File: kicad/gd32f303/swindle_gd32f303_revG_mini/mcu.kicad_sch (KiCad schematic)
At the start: 23 parts, among them J40 J40, J7 Conn_01x05_Pin, Q1 DMG2302U, U1 GD32F303, Y2 8Mhz

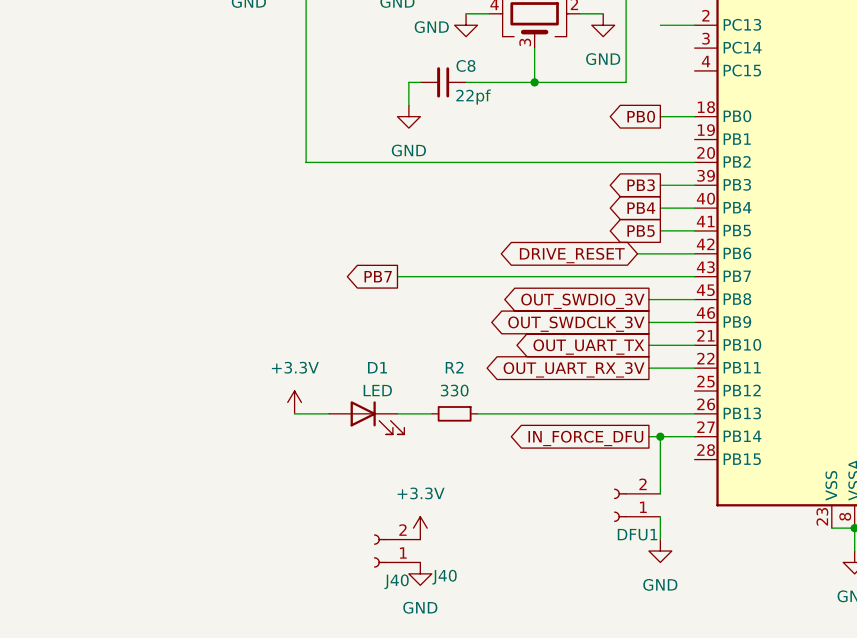
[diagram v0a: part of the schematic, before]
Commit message: kicad: add pullup resistor on GD32/48 version
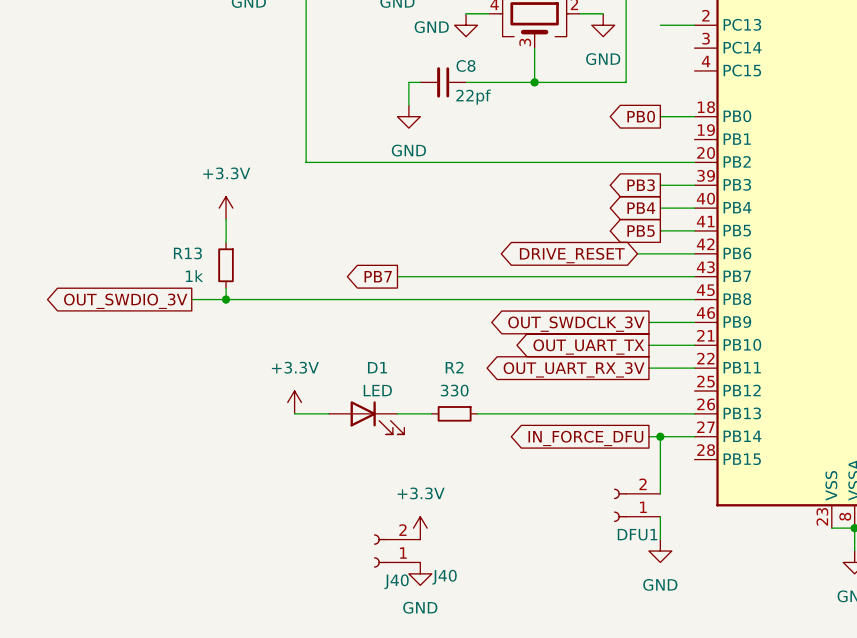
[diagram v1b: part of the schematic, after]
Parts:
- added R13: 1k, Resistor_SMD:R_0603_1608Metric, symbol Device:R_Small
- J8: value ~ -> (none)
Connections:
- net +3.3V: now also R13.1
- net OUT_SWDIO_3V: now also R13.2
